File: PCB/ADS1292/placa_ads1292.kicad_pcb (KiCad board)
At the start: 2 copper layers, 14 parts, among them P2 CONN_02X07, U3 ADS1292

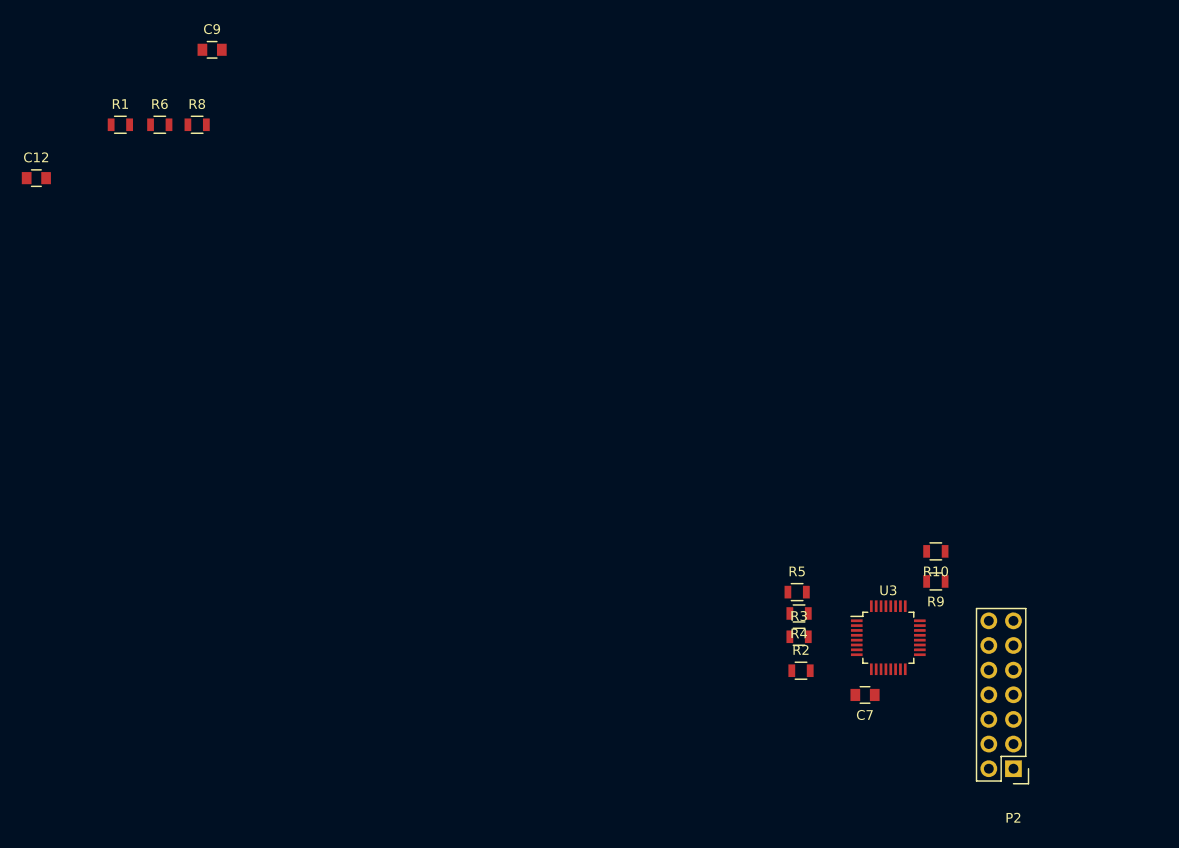
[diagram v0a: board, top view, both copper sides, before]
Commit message: Terminé de rutear la placa con el ADS1292. Habría que cambiar el conector de cable plano por uno de 2 mm.
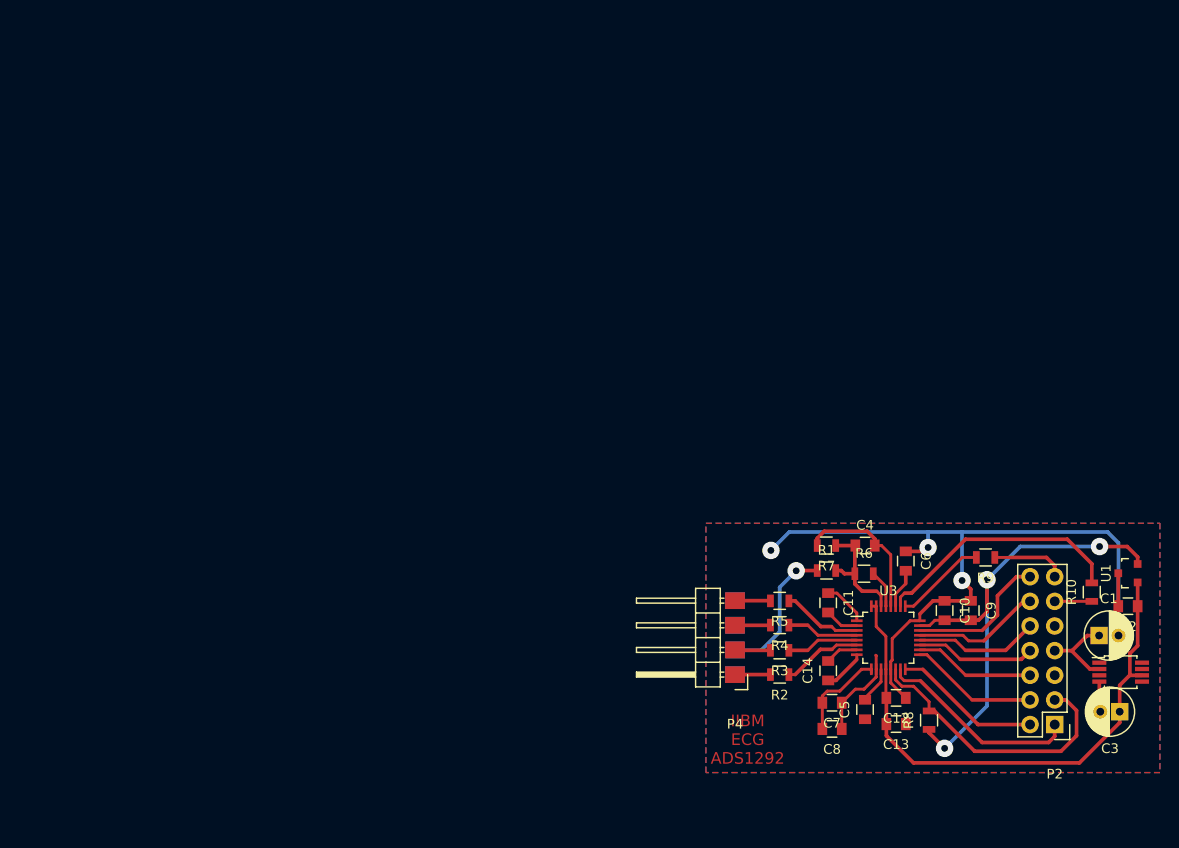
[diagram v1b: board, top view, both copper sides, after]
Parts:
- added C1: 1u, Capacitors_ThroughHole:C_Radial_D5_L11_P2, F.Cu at (139.6, 78.5)
- added C10: 1u, Capacitors_SMD:C_0805, F.Cu at (123.7, 75.9)
- added C11: 4.7n, Capacitors_SMD:C_0805, F.Cu at (111.7, 75.1)
- added C13: 1u, Capacitors_SMD:C_0805, F.Cu at (118.7, 87.6)
- added C14: 4.7n, Capacitors_SMD:C_0805, F.Cu at (111.7, 82.1)
- added C2: 0.47u, Capacitors_SMD:C_0805, F.Cu at (142.6, 75.5)
- added C3: 1u, Capacitors_ThroughHole:C_Radial_D5_L11_P2, F.Cu at (141.8, 86.3)
- added C4: 1.5n, Capacitors_SMD:C_0805, F.Cu at (115.5, 69.2)
- added C5: 1u, Capacitors_SMD:C_0805, F.Cu at (115.5, 86.1)
- added C6: 1u, Capacitors_SMD:C_0805, F.Cu at (119.7, 70.8)
- added C8: 1u, Capacitors_SMD:C_0805, F.Cu at (112.1, 88.1)
- added P3: CONN_01X04, Pin_Headers:Pin_Header_Angled_1x04, B.Cu at (102.1, 74.9)
- added P4: CONN_01X04, Pin_Headers:Pin_Header_Angled_1x04, F.Cu at (102.1, 82.5)
- added R7: 1M, Resistors_SMD:R_0805, F.Cu at (111.5, 69.2)
- added U1: REF3133, TO_SOT_Packages_SMD:SOT-23, F.Cu at (142.6, 72.0)
- added U2: REF5050, Housings_SSOP:MSOP-8_3x3mm_Pitch0.65mm, F.Cu at (141.8, 82.2)
- moved C12 103.6 mm to (118.7, 84.9), turned to 180 degrees
- moved R8 97.3 mm to (122.1, 87.2), turned to 90 degrees
- moved C9 97.2 mm to (126.4, 75.9), turned to 270 degrees
- moved R6 86.1 mm to (115.4, 72.1)
- moved R1 86.1 mm to (111.5, 71.8)
- moved R10 16.6 mm to (138.9, 74.0), turned to 90 degrees
- moved P2 6.23 mm to (135.1, 87.7)
- moved R9 5.69 mm to (127.9, 70.4)
- moved C7 3.49 mm to (112.1, 85.4)
- moved R3 2.44 mm to (106.7, 80.0), turned to 180 degrees
- moved R4 2.33 mm to (106.7, 77.4)
- moved R2 2.24 mm to (106.7, 82.5), turned to 180 degrees
- moved R5 2.01 mm to (106.7, 74.9), turned to 180 degrees
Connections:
- P2 pad 1: (no net) -> Net-(P2-Pad1)
- P2 pad 3: (no net) -> Net-(P2-Pad3)
- P2 pad 7: Net-(P2-Pad7) -> +BATT
- P2 pad 9: Net-(P2-Pad9) -> GND
- R1 pad 1: (no net) -> Net-(P3-Pad3)
- R10 pad 1: Net-(P2-Pad13) -> Net-(P2-Pad11)
- R2 pad 2: (no net) -> Net-(P4-Pad1)
- R3 pad 2: (no net) -> Net-(P4-Pad2)
- R4 pad 2: (no net) -> Net-(P4-Pad3)
- R5 pad 2: (no net) -> Net-(P4-Pad4)
- R8 pad 2: Net-(P2-Pad2) -> Net-(P2-Pad3)
- R9 pad 1: Net-(P2-Pad11) -> Net-(P2-Pad13)
- U3 pad 1: (no net) -> Net-(C11-Pad1)
- U3 pad 11: (no net) -> Net-(C5-Pad2)
- U3 pad 14: Net-(P2-Pad2) -> Net-(P2-Pad3)
- U3 pad 15: Net-(P2-Pad4) -> Net-(P2-Pad1)
- U3 pad 16: Net-(P2-Pad6) -> Net-(P2-Pad2)
- U3 pad 17: Net-(P2-Pad8) -> Net-(P2-Pad4)
- U3 pad 18: Net-(P2-Pad10) -> Net-(P2-Pad6)
- U3 pad 19: Net-(P2-Pad12) -> Net-(P2-Pad8)
- U3 pad 2: (no net) -> Net-(C11-Pad2)
- U3 pad 20: Net-(P2-Pad14) -> Net-(P2-Pad10)
- U3 pad 21: Net-(P2-Pad7) -> Net-(P2-Pad12)
- U3 pad 22: Net-(P2-Pad9) -> Net-(P2-Pad14)
- U3 pad 27: (no net) -> Net-(C6-Pad2)
- U3 pad 28: (no net) -> Net-(C4-Pad2)
- U3 pad 31: /AVDD -> +5V
- U3 pad 32: /AVDD -> +5V
- U3 pad 7: (no net) -> Net-(C14-Pad2)
- U3 pad 8: (no net) -> Net-(C14-Pad1)
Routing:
- net GND: track 0.00 -> 91.5 mm, vias 0 -> 3
- net +5V: track 0.00 -> 57.7 mm
- net +3V3: track 0.00 -> 50.7 mm, vias 0 -> 3
- net Net-(P2-Pad3): track 0.00 -> 29.3 mm
- net Net-(R10-Pad2): track 0.00 -> 26.1 mm
- net Net-(P2-Pad1): track 0.00 -> 21.0 mm
- net Net-(C4-Pad2): track 0.00 -> 15.3 mm
- net Net-(P2-Pad2): track 0.00 -> 15.2 mm
- net Net-(P2-Pad14): track 0.00 -> 14.8 mm
- net Net-(P3-Pad3): track 0.00 -> 14.6 mm, vias 0 -> 1
- net Net-(P2-Pad4): track 0.00 -> 13.3 mm
- net Net-(P2-Pad12): track 0.00 -> 13.3 mm
- net Net-(P2-Pad10): track 0.00 -> 12.8 mm
- net Net-(C4-Pad1): track 0.00 -> 12.5 mm
- net Net-(P2-Pad6): track 0.00 -> 12.4 mm
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- added copper zone on B.Cu, net GND
- added copper zone on F.Cu, net GND
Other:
- net class Default: clearance 0.2 -> 0.1778; trace_width 0.25 -> 0.3048; via_dia 0.6 -> 1.8; via_drill 0.4 -> 0.7
- rule trace_clearance: 0.2 -> 0.1778
- board text added: "IIBM ECG ADS1292"

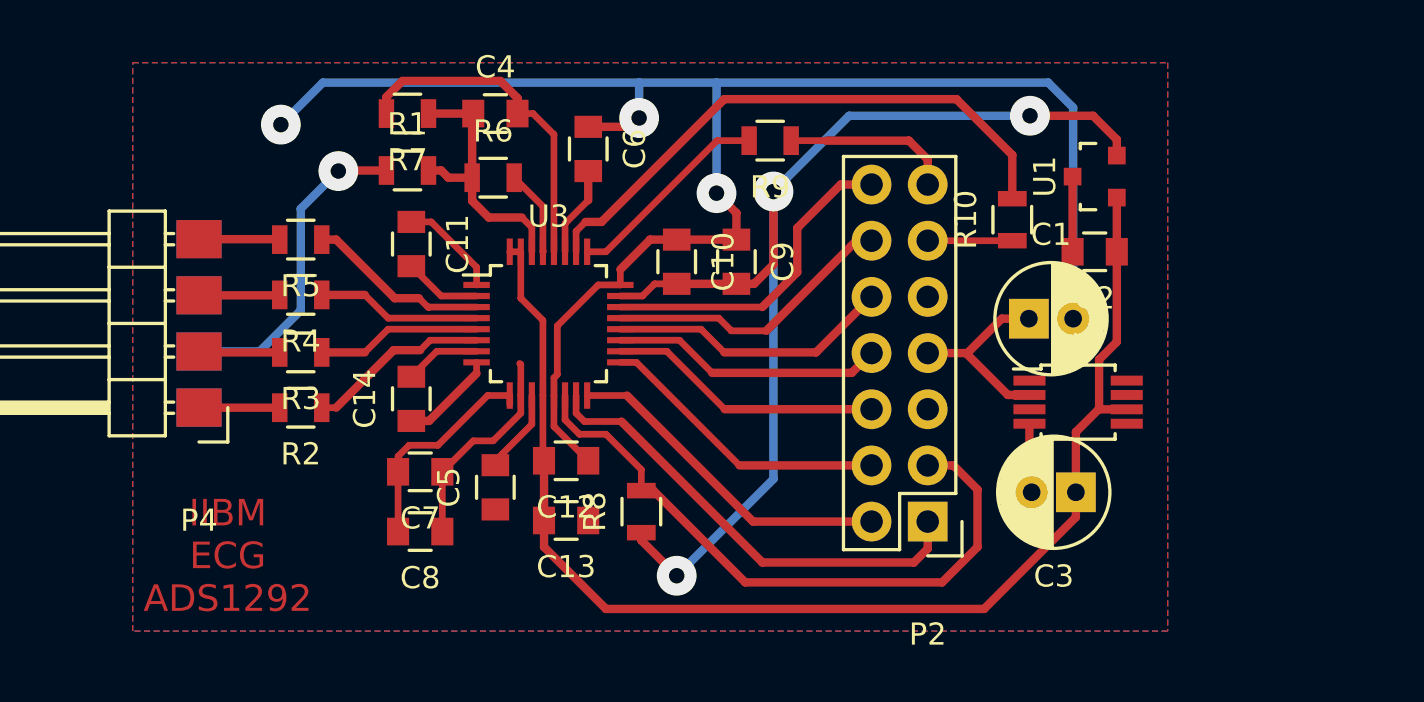
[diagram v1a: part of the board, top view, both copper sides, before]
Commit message: Modifico la placa con el das1292 para cambiarle el regulador de 3.3V
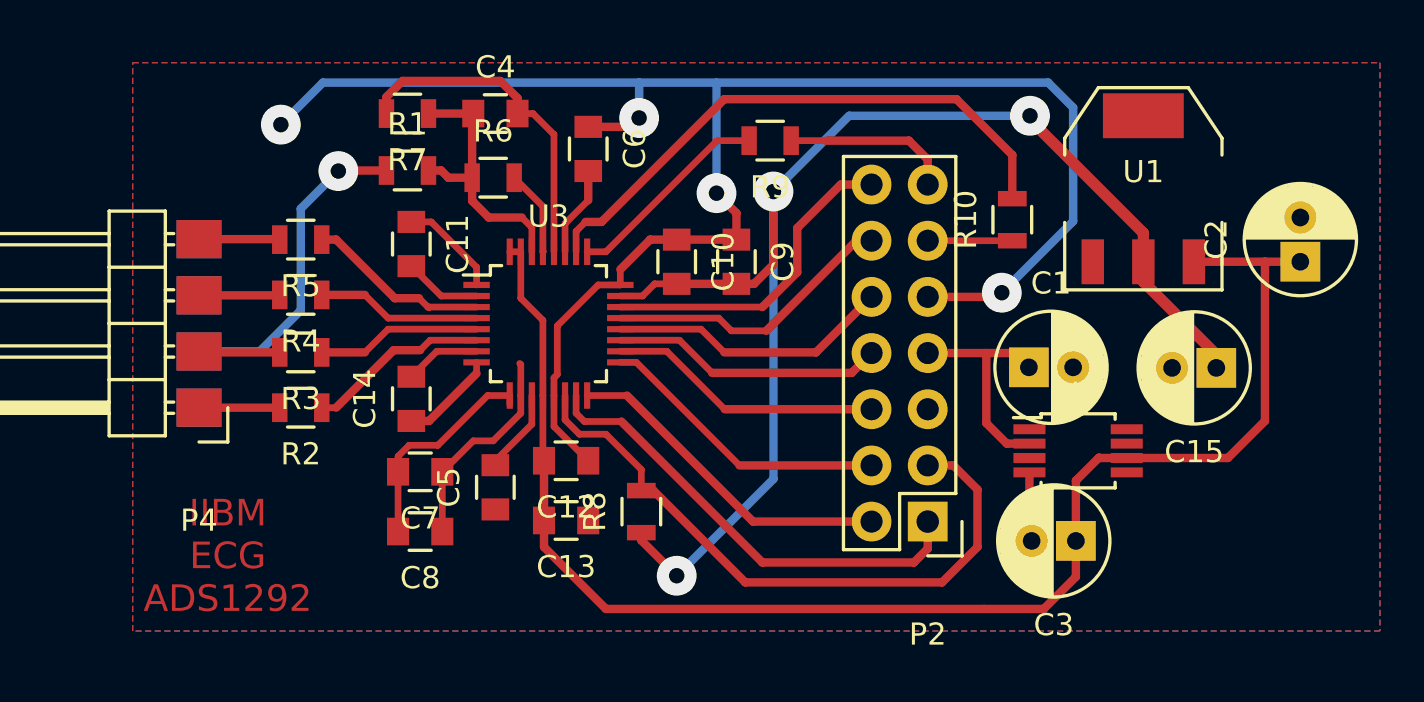
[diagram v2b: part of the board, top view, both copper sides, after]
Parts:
- added C15: 10u, Capacitors_ThroughHole:C_Radial_D5_L11_P2, F.Cu at (148.1, 80.7)
- C2: value 0.47u -> 10u; footprint Capacitors_SMD:C_0805 -> Capacitors_ThroughHole:C_Radial_D5_L11_P2
- U1: value REF3133 -> AIC1117-33; footprint TO_SOT_Packages_SMD:SOT-23 -> TO_SOT_Packages_SMD:SOT-223
- moved C2 9.31 mm to (151.9, 75.9), turned to 90 degrees
- moved U1 2.27 mm to (144.8, 72.6), turned to 0 degrees
- moved C1 2.20 mm to (139.6, 80.7)
- moved C3 2.20 mm to (141.8, 88.5)
- moved U2 2.20 mm to (141.8, 84.5)
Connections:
- U1 pad 1: +5V -> GND
- U1 pad 3: GND -> +5V
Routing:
- net +3V3: track 50.7 -> 61.1 mm
- net +5V: track 57.7 -> 66.2 mm
- net +BATT: track 8.87 -> 10.3 mm
- net GND: track 91.5 -> 91.6 mm, vias 3 -> 4

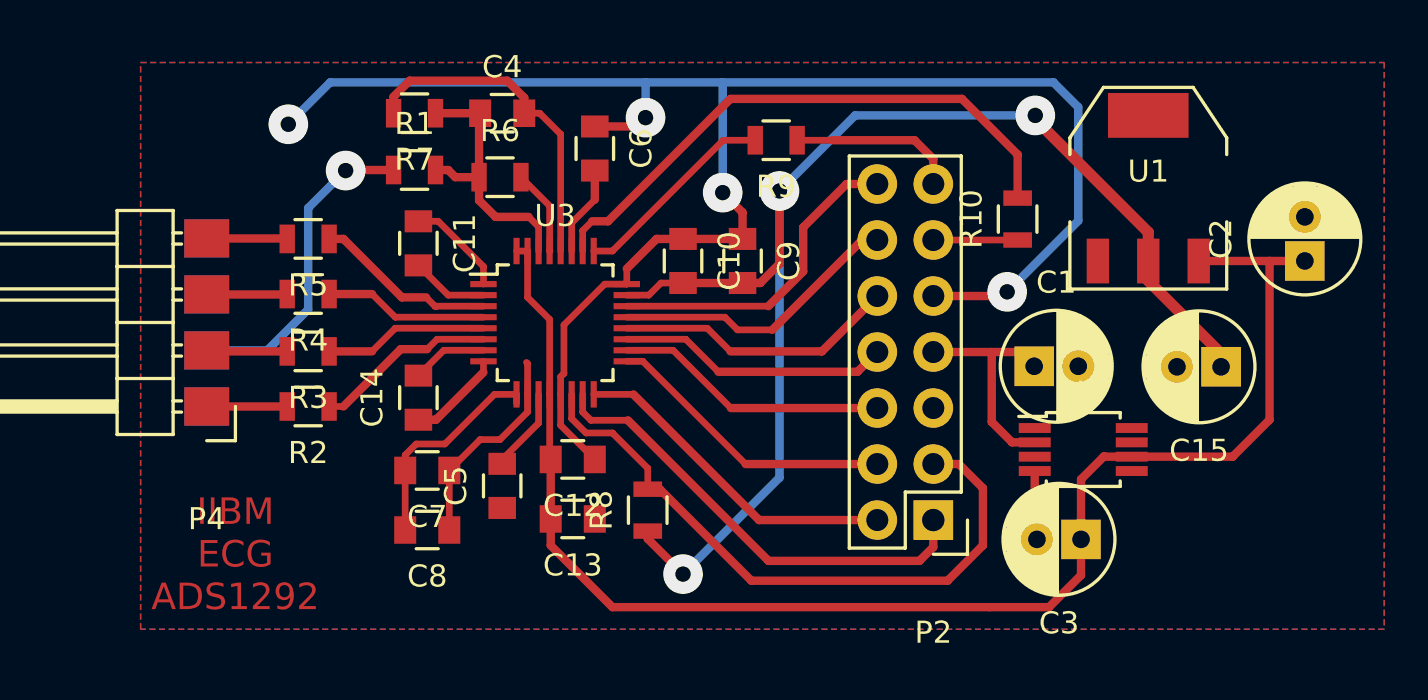
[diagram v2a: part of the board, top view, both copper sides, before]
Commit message: Cambio unas cosas en la placa
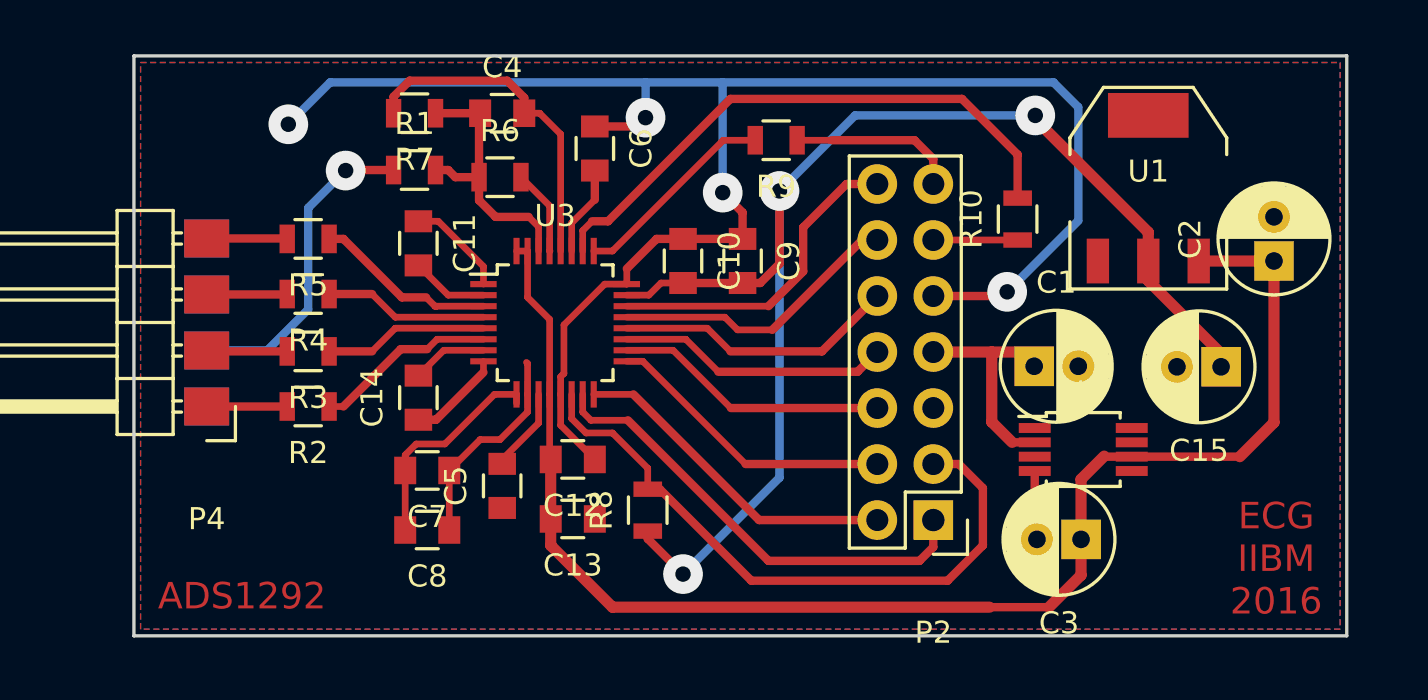
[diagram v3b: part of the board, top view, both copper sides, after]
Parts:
- moved C2 1.40 mm to (150.5, 75.9)
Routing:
- net +5V: track 66.2 -> 65.1 mm
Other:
- board outline added: 55 x 26.3 mm
- board text added: "ADS1292"
- board text added: "ECG IIBM 2016"
- board text removed: "IIBM ECG ADS1292"

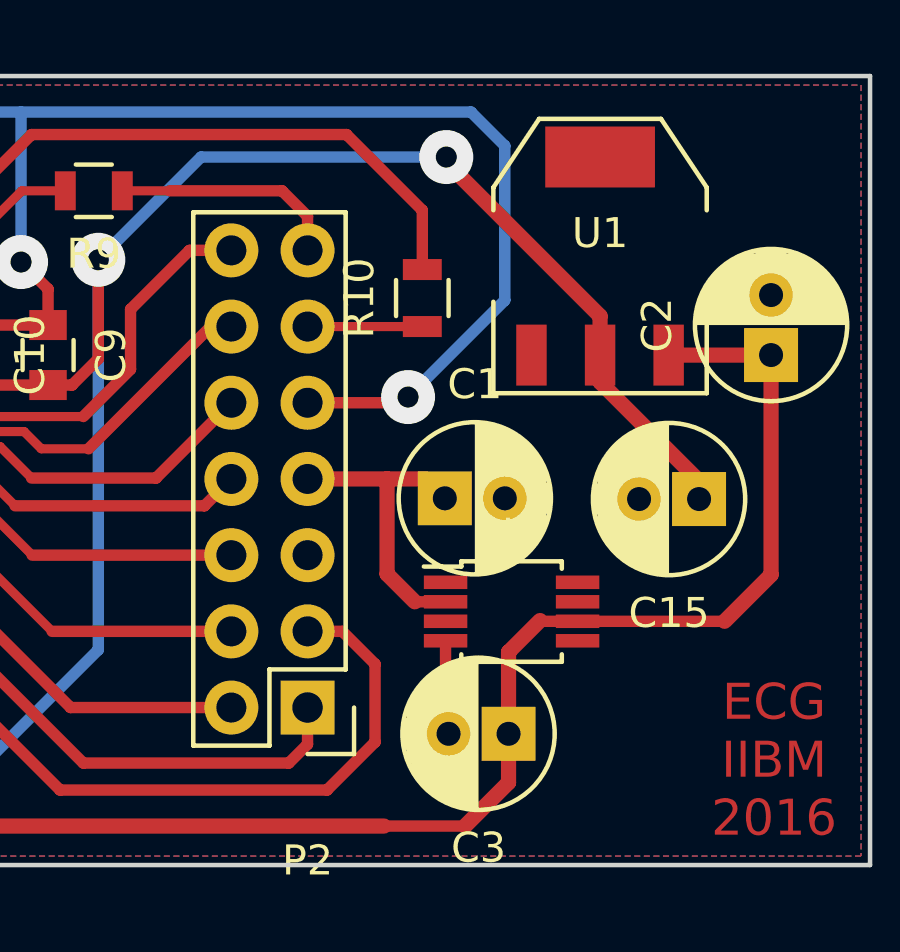
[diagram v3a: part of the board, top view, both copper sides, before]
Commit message: Modifico la posición del conector para que quede como en el cable.
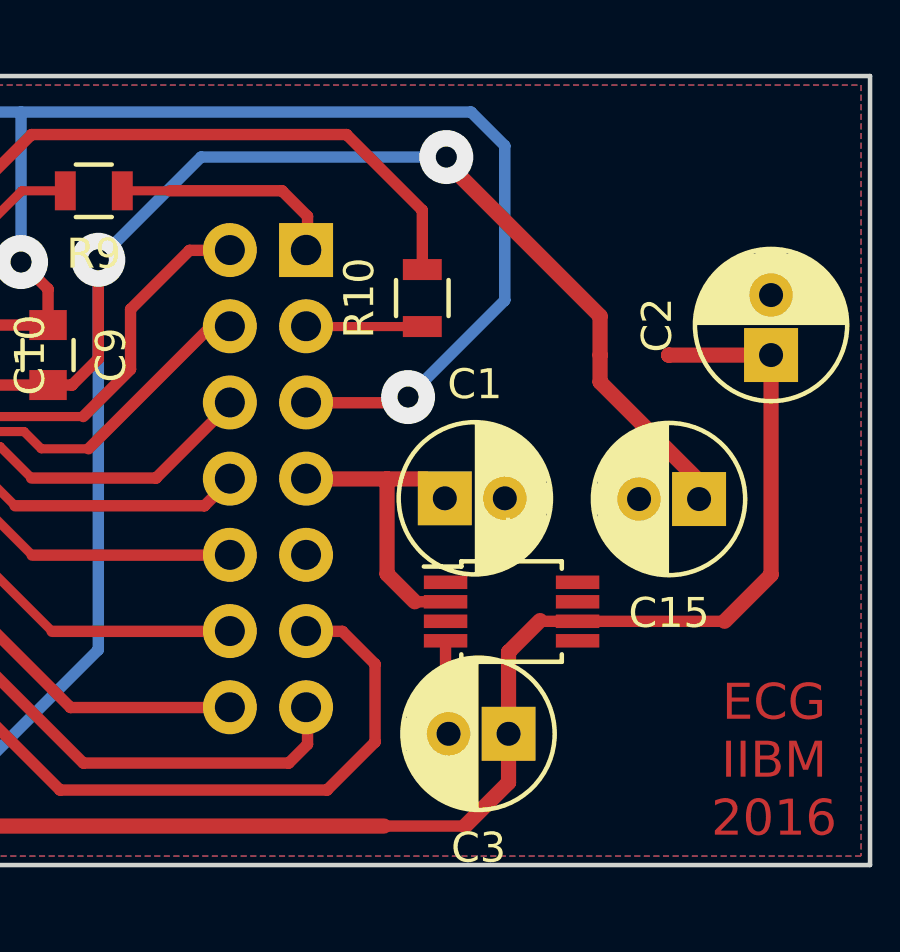
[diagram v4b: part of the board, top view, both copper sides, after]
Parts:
- removed U1: AIC1117-33, TO_SOT_Packages_SMD:SOT-223
- P2: moved to B.Cu
- moved P2 15.3 mm to (135.0, 72.4)
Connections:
- P2 pad 5: (no net) -> GND
- P2 pad 9: GND -> Net-(P2-Pad9)
- P3 pad 1: (no net) -> Net-(P3-Pad1)
- P3 pad 2: (no net) -> Net-(P3-Pad2)
- P3 pad 4: (no net) -> Net-(P3-Pad4)
- R10 pad 1: Net-(P2-Pad11) -> Net-(P2-Pad3)
- R8 pad 2: Net-(P2-Pad3) -> Net-(P2-Pad11)
- R9 pad 1: Net-(P2-Pad13) -> Net-(P2-Pad1)
- U2 pad 3: (no net) -> Net-(U2-Pad3)
- U2 pad 5: (no net) -> Net-(U2-Pad5)
- U3 pad 14: Net-(P2-Pad3) -> Net-(P2-Pad11)
- U3 pad 15: Net-(P2-Pad1) -> Net-(P2-Pad13)
- U3 pad 16: Net-(P2-Pad2) -> Net-(P2-Pad14)
- U3 pad 17: Net-(P2-Pad4) -> Net-(P2-Pad12)
- U3 pad 18: Net-(P2-Pad6) -> Net-(P2-Pad10)
- U3 pad 20: Net-(P2-Pad10) -> Net-(P2-Pad6)
- U3 pad 21: Net-(P2-Pad12) -> Net-(P2-Pad4)
- U3 pad 22: Net-(P2-Pad14) -> Net-(P2-Pad2)
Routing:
- net Net-(P2-Pad3): track 29.3 -> 3.82 mm
- net Net-(P2-Pad11): track 3.82 -> 29.3 mm
- net Net-(P2-Pad1): track 21.0 -> 7.66 mm
- net Net-(P2-Pad13): track 7.66 -> 21.0 mm
